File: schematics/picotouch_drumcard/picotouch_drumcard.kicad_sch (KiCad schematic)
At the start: 80 parts, among them J1 AudioJack4, J2 AudioJack4, J3 AudioJack4, SW1 Capacitive Button, SW10 Capacitive Button, SW11 Capacitive Button, SW12 Capacitive Button, SW13 Capacitive Button, SW14 Capacitive Button, SW15 Capacitive Button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

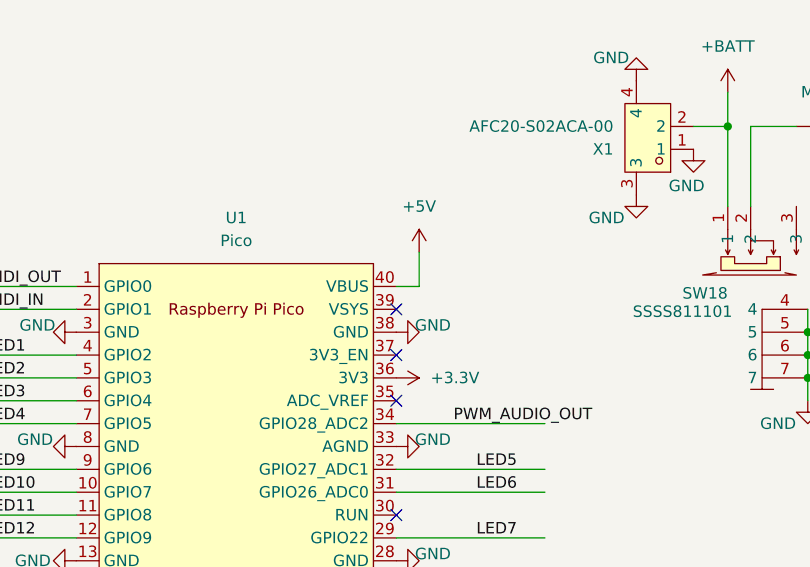
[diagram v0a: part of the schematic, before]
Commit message: sigh more fixes to charging circuit
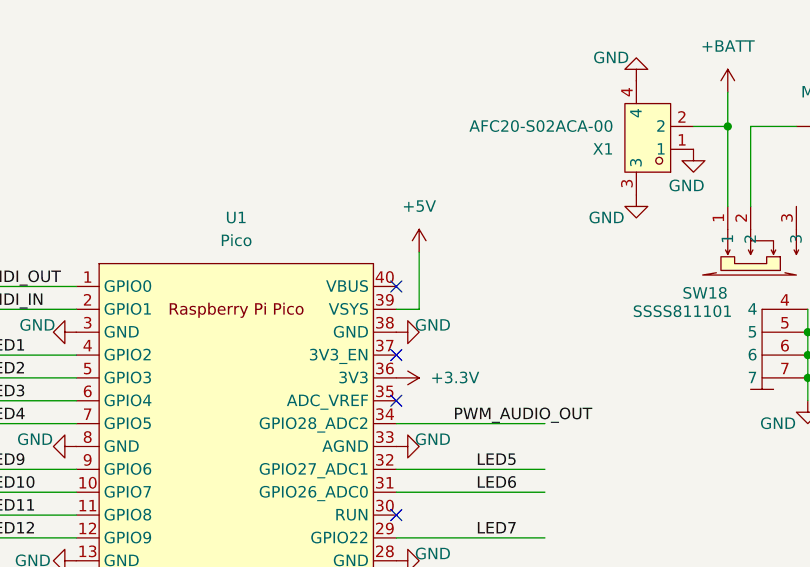
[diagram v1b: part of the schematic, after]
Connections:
- net +5V: now also U1.39 (VSYS); no longer U1.40 (VBUS)
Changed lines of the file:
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@@
-	)
-	(no_connect
-		(at 77.47 48.26)
 	)
 	(no_connect
@@
 	)
 	(no_connect
+		(at 77.47 45.72)
+	)
+	(no_connect
 		(at 157.48 153.67)
 	)
@@
 	(wire
 		(pts
+			(xy 77.47 48.26) (xy 80.01 48.26)
+		)
+		(stroke
+			(width 0)
+			(type default)
+		)
+	)
+	(wire
+		(pts
 			(xy 87.63 132.08) (xy 87.63 129.54)
 		)
@@
 	(wire
 		(pts
-			(xy 80.01 45.72) (xy 77.47 45.72)
-		)
-		(stroke
-			(width 0)
-			(type default)
-		)
-	)
-	(wire
-		(pts
 			(xy 187.96 96.52) (xy 201.93 96.52)
 		)
@@
 	(wire
 		(pts
-			(xy 80.01 41.91) (xy 80.01 45.72)
-		)
-		(stroke
-			(width 0)
-			(type default)
-		)
-	)
-	(wire
-		(pts
 			(xy 29.21 91.44) (xy 41.91 91.44)
 		)
@@
 		)
 		(stroke
+			(width 0)
+			(type default)
+		)
+	)
+	(wire
+		(pts
+			(xy 80.01 41.91) (xy 80.01 48.26)
+		)
+		(stroke

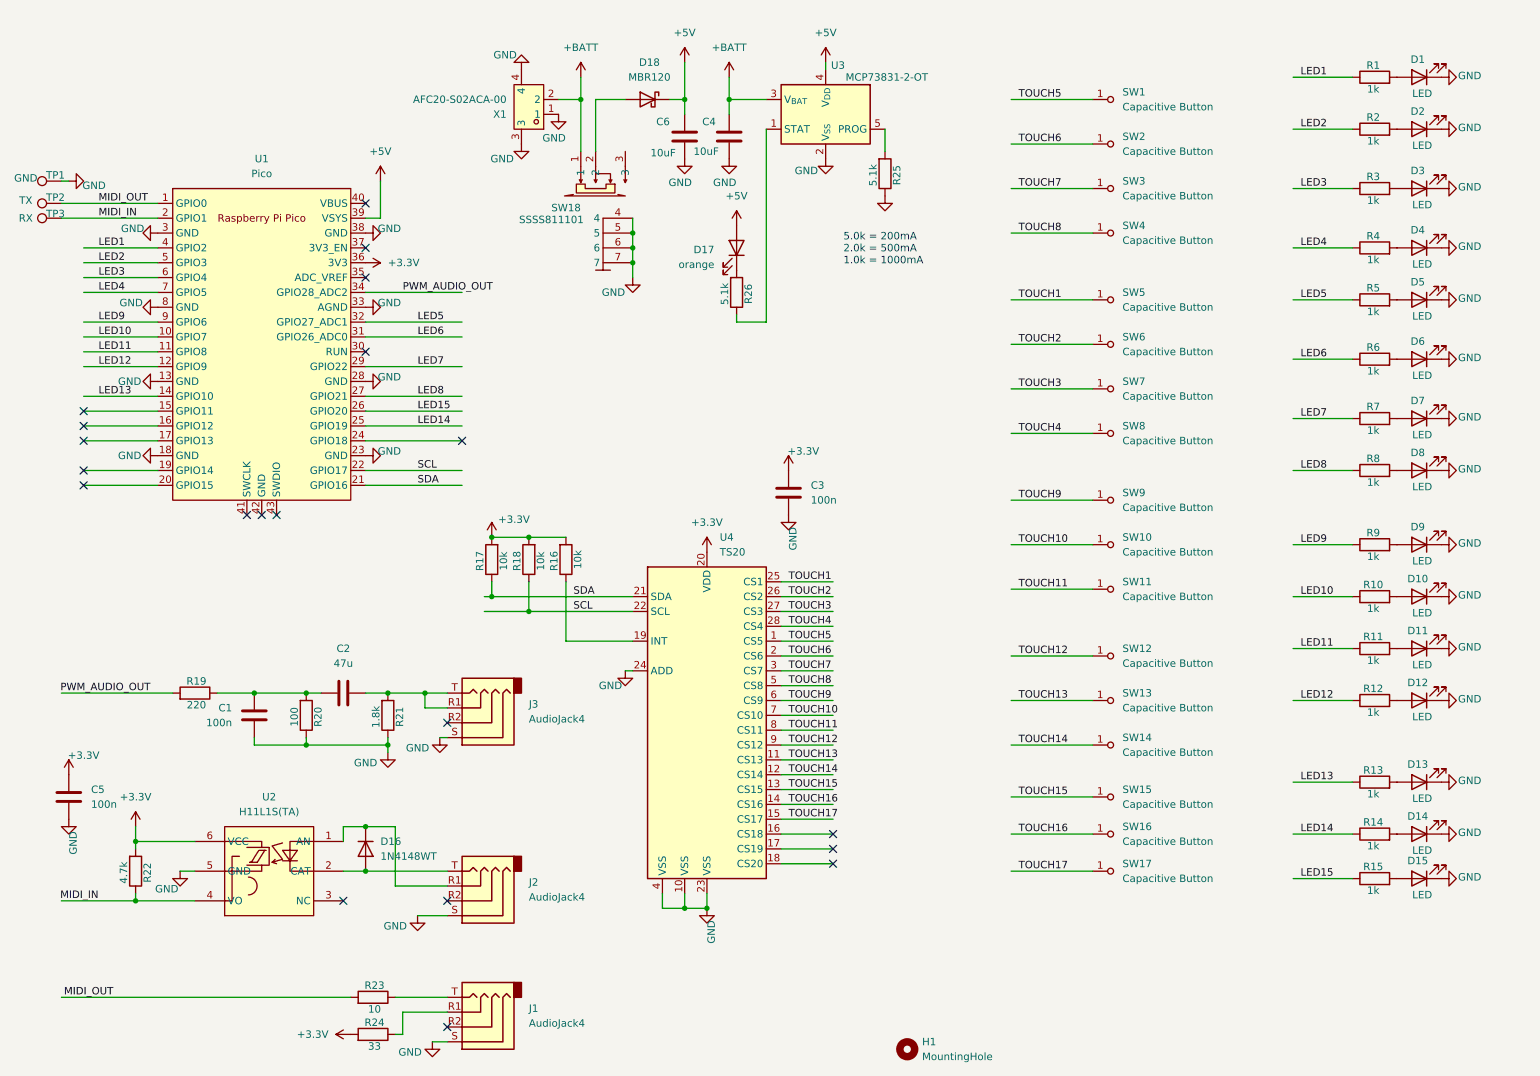
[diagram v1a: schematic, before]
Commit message: audio out needs Ring2 to Gnd for headphones to work (I knew this)
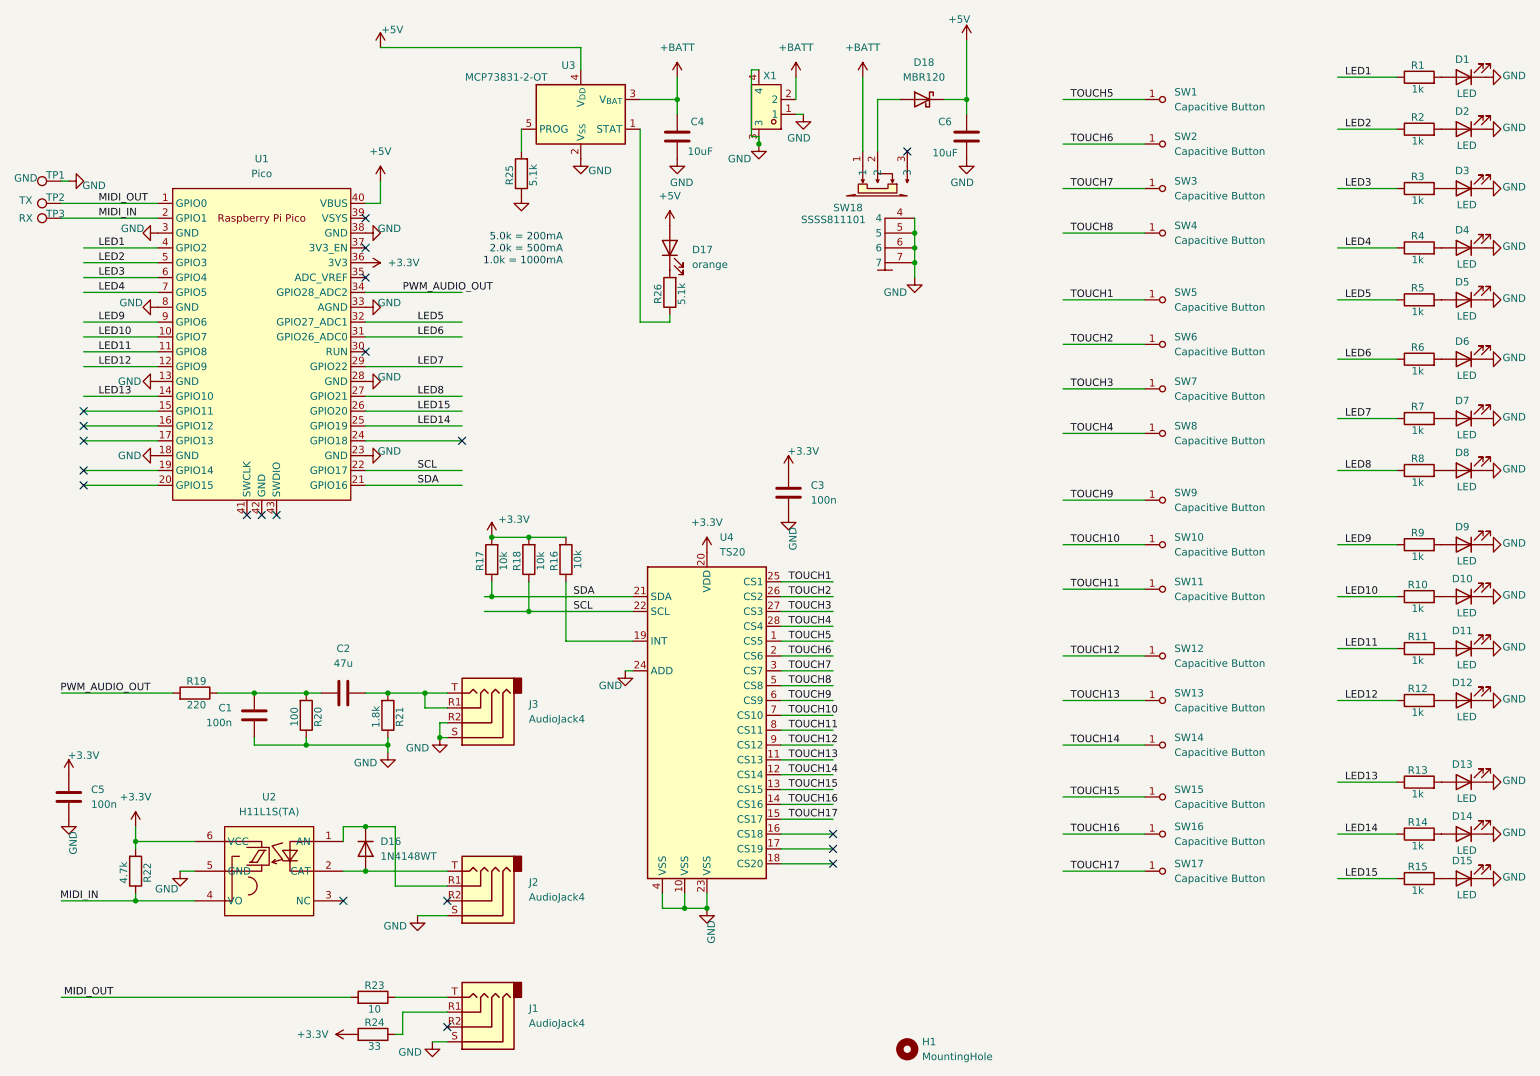
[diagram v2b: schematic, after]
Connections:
- net +5V: now also U1.40 (VBUS); no longer U1.39 (VSYS)
- net GND: now also J3.R2
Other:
- moved on the sheet: C4, C6, D1, D10, D11, D12, D13, D14, D15, D17, D18, D2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
